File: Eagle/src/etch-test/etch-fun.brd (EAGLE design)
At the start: 2 parts

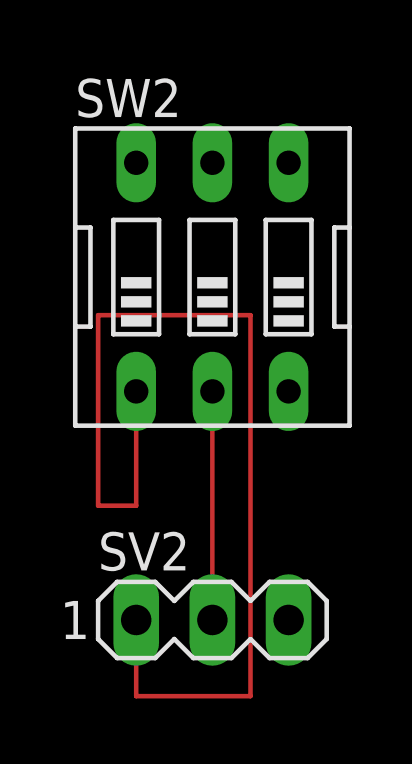
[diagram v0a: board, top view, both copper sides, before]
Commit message: Update etch-fun.brd
small test PCB
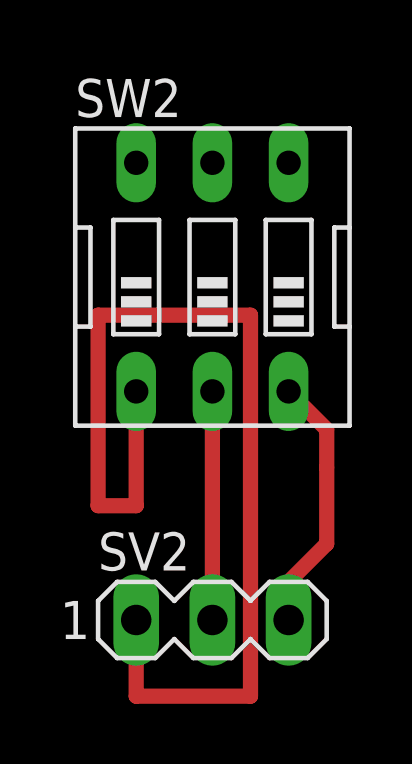
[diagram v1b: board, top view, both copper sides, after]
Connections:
- new net N$3: SV2.3, SW2.3
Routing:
- net N$3: track 0.00 -> 8.67 mm
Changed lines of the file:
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@@
 </variantdefs>
 <classes>
-<class number="0" name="default" width="0" drill="0">
+<class number="0" name="default" width="0.254" drill="0">
+</class>
+<class number="1" name="test1" width="0.3048" drill="0">
 </class>
 </classes>
@@
 <contactref element="SV2" pad="1"/>
 <contactref element="SW2" pad="1"/>
-<wire x1="5.08" y1="3.81" x2="5.08" y2="1.27" width="0.1524" layer="1"/>
-<wire x1="5.08" y1="1.27" x2="8.89" y2="1.27" width="0.1524" layer="1"/>
-<wire x1="8.89" y1="1.27" x2="8.89" y2="13.97" width="0.1524" layer="1"/>
-<wire x1="3.81" y1="13.97" x2="3.81" y2="7.62" width="0.1524" layer="1"/>
-<wire x1="3.81" y1="7.62" x2="5.08" y2="7.62" width="0.1524" layer="1"/>
-<wire x1="5.08" y1="7.62" x2="5.08" y2="11.43" width="0.1524" layer="1"/>
-<wire x1="8.89" y1="13.97" x2="3.81" y2="13.97" width="0.1524" layer="1"/>
+<wire x1="5.08" y1="3.81" x2="5.08" y2="1.27" width="0.508" layer="1"/>
+<wire x1="5.08" y1="1.27" x2="8.89" y2="1.27" width="0.508" layer="1"/>
+<wire x1="8.89" y1="1.27" x2="8.89" y2="13.97" width="0.508" layer="1"/>
+<wire x1="3.81" y1="13.97" x2="3.81" y2="7.62" width="0.508" layer="1"/>
+<wire x1="3.81" y1="7.62" x2="5.08" y2="7.62" width="0.508" layer="1"/>
+<wire x1="5.08" y1="7.62" x2="5.08" y2="11.43" width="0.508" layer="1"/>
+<wire x1="8.89" y1="13.97" x2="3.81" y2="13.97" width="0.508" layer="1"/>
 </signal>
 <signal name="N$2">
 <contactref element="SW2" pad="2"/>
 <contactref element="SV2" pad="2"/>
-<wire x1="7.62" y1="3.81" x2="7.62" y2="11.43" width="0.1524" layer="1"/>
+<wire x1="7.62" y1="3.81" x2="7.62" y2="11.43" width="0.508" layer="1"/>
+</signal>
+<signal name="N$3">
+<contactref element="SV2" pad="3"/>
+<contactref element="SW2" pad="3"/>
+<wire x1="10.16" y1="3.81" x2="10.16" y2="5.08" width="0.508" layer="1"/>
+<wire x1="10.16" y1="5.08" x2="11.43" y2="6.35" width="0.508" layer="1"/>
+<wire x1="11.43" y1="6.35" x2="11.43" y2="8.89" width="0.508" layer="1"/>
+<wire x1="11.43" y1="8.89" x2="11.43" y2="10.16" width="0.508" layer="1"/>
+<wire x1="11.43" y1="10.16" x2="10.16" y2="11.43" width="0.508" layer="1"/>
+<wire x1="11.43" y1="8.89" x2="11.43" y2="8.89" width="0.508" layer="1"/>
 </signal>
 </signals>
